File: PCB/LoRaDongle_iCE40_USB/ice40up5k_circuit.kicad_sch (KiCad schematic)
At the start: 41 parts, among them IC3 SGP40-D-R4, J3 Conn_01x08_Male, J4 Conn_01x04_Male, J6 Conn_02x02_Top_Bottom, J9 Conn_01x17_Male, SW1 SW_Push, SW2 SW_Push, U5 W25Q128JVS, U6 ICE40UP5K-SG48ITR, X1 ECS-2520MV-500-BL-TR

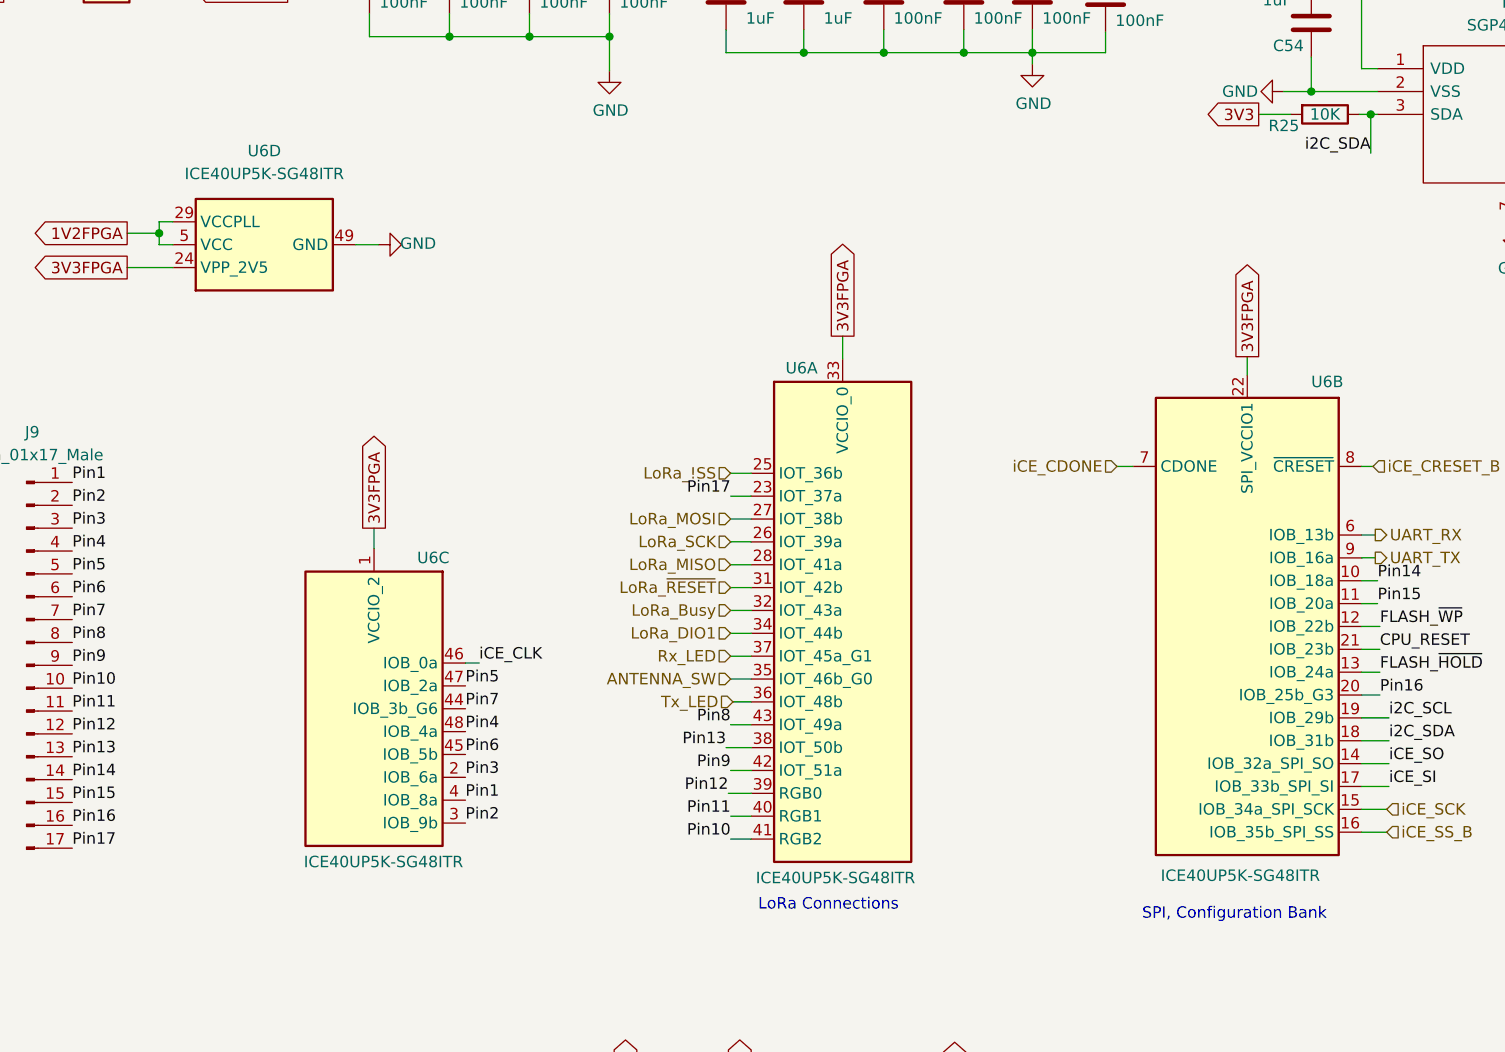
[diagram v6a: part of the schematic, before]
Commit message: updated silkscreen
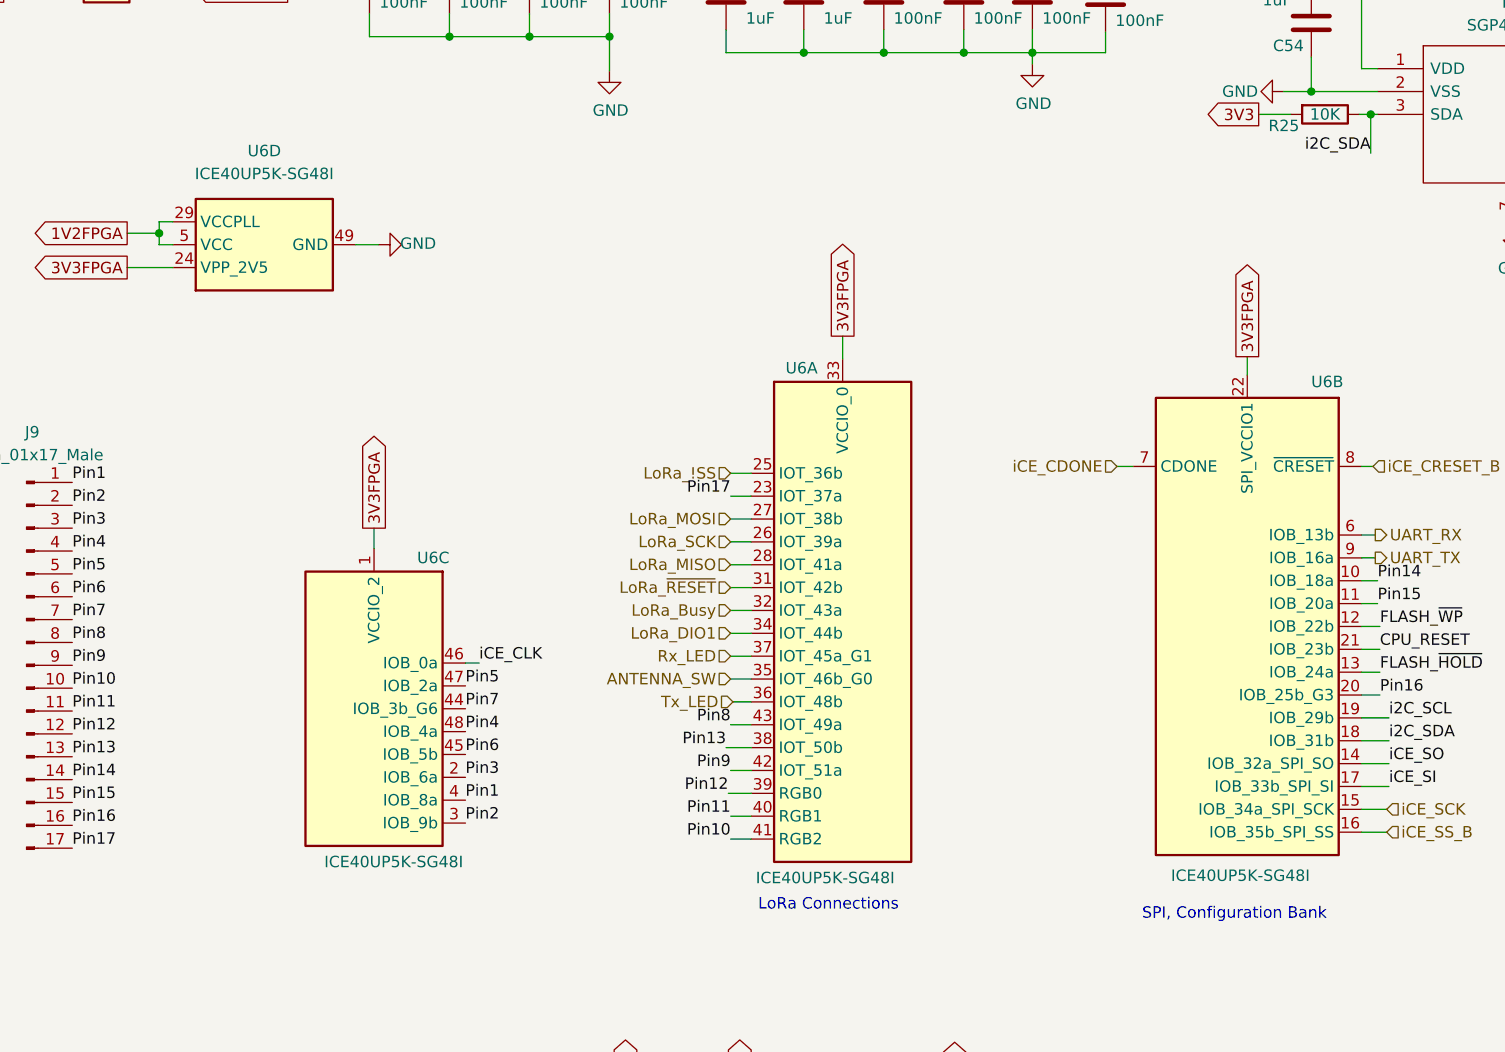
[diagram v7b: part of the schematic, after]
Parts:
- D2, IC3, R12, R13, R14, R15, R16, R17, R24, R25, R26, R27, U5: Type (none) -> SMD
- J3, J4, J9: Type (none) -> Through Hole
- J6: Type (none) -> Through hole
- U6: value ICE40UP5K-SG48ITR -> ICE40UP5K-SG48I; Manufacturer Part Number ICE40UP5K-SG48ITR50 -> ICE40UP5K-SG48IT; Type (none) -> SMD
- iCE_CLK1: Type (none) -> -
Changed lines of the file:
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@@
+      (effects (font (size 1.27 1.27)) hide)
+    )
+    (property "Type" "SMD" (id 8) (at 107.696 164.592 0)
       (effects (font (size 1.27 1.27)) hide)
     )
@@
       (effects (font (size 1.27 1.27)) hide)
     )
+    (property "Type" "SMD" (id 8) (at 94.996 164.592 0)
+      (effects (font (size 1.27 1.27)) hide)
+    )
     (pin "1")
     (pin "2")
@@
     )
     (property "Package" "0603" (id 7) (at 94.996 181.102 0)
+      (effects (font (size 1.27 1.27)) hide)
+    )
+    (property "Type" "SMD" (id 8) (at 94.996 181.102 0)
       (effects (font (size 1.27 1.27)) hide)
     )
@@
       (effects (font (size 1.27 1.27)) hide)
     )
+    (property "Type" "SMD" (id 8) (at 220.98 85.852 0)
+      (effects (font (size 1.27 1.27)) hide)
+    )
     (pin "1")
     (pin "2")
@@
       (effects (font (size 1.27 1.27)) hide)
     )
+    (property "Type" "SMD" (id 8) (at 271.272 102.362 0)
+      (effects (font (size 1.27 1.27)) hide)
+    )
     (pin "1")
     (pin "2")
@@
       (effects (font (size 1.27 1.27)) hide)
     )
+    (property "Type" "SMD" (id 8) (at 271.272 99.822 0)
+      (effects (font (size 1.27 1.27)) hide)
+    )
     (pin "1")
     (pin "2")
@@
       (effects (font (size 1.27 1.27)) hide)
     )
+    (property "Type" "SMD" (id 8) (at 225.552 85.852 0)
+      (effects (font (size 1.27 1.27)) hide)
+    )
     (pin "1")
     (pin "2")
@@
       (effects (font (size 1.27 1.27)) (justify left))
     )
-    (property "Value" "ICE40UP5K-SG48ITR" (id 1) (at 109.474 133.35 0)
+    (property "Value" "ICE40UP5K-SG48I" (id 1) (at 109.474 133.35 0)
       (effects (font (size 1.27 1.27)) (justify left))
     )
@@
       (effects (font (size 1.27 1.27)) hide)
     )
-    (property "Manufacturer Part Number" "ICE40UP5K-SG48ITR50" (id 5) (at 119.126 103.632 0)
+    (property "Manufacturer Part Number" "ICE40UP5K-SG48IT" (id 5) (at 119.126 103.632 0)
       (effects (font (size 1.27 1.27)) hide)
     )
     (property "Package" "48-QFN" (id 6) (at 119.126 103.632 0)
+      (effects (font (size 1.27 1.27)) hide)
+    )
+    (property "Type" "SMD" (id 7) (at 119.126 103.632 0)
       (effects (font (size 1.27 1.27)) hide)
     )
@@
       (effects (font (size 1.27 1.27)) hide)
     )
+    (property "Type" "SMD" (id 8) (at 214.376 36.576 0)
+      (effects (font (size 1.27 1.27)) hide)
+    )
     (pin "1")
     (pin "2")
@@
       (effects (font (size 1.27 1.27)) hide)
     )
+    (property "Type" "Through hole" (id 8) (at 36.068 32.258 0)
+      (effects (font (size 1.27 1.27)) hide)
+    )
     (pin "1")
     (pin "2")
@@
     (in_bom yes) (on_board yes)
     (property "Reference" "U6" (id 0) (at 172.974 78.232 0))
-    (property "Value" "ICE40UP5K-SG48ITR" (id 1) (at 163.322 133.096 0))
+    (property "Value" "ICE40UP5K-SG48I" (id 1) (at 163.322 133.096 0))
     (property "Footprint" "Package_DFN_QFN:QFN-48-1EP_7x7mm_P0.5mm_EP5.6x5.6mm" (id 2) (at 164.084 139.7 0)
       (effects (font (size 1.27 1.27)) hide)
@@
       (effects (font (size 1.27 1.27)) hide)
     )
-    (property "Manufacturer Part Number" "ICE40UP5K-SG48ITR50" (id 5) (at 164.084 105.41 0)
+    (property "Manufacturer Part Number" "ICE40UP5K-SG48IT" (id 5) (at 164.084 105.41 0)
       (effects (font (size 1.27 1.27)) hide)
     )
     (property "Package" "48-QFN" (id 6) (at 164.084 105.41 0)
+      (effects (font (size 1.27 1.27)) hide)
+    )
+    (property "Type" "SMD" (id 7) (at 164.084 105.41 0)
       (effects (font (size 1.27 1.27)) hide)
     )
@@
     (in_bom yes) (on_board yes) (fields_autoplaced)
     (property "Reference" "U6" (id 0) (at 54.864 52.578 90))
-    (property "Value" "ICE40UP5K-SG48ITR" (id 1) (at 54.864 55.118 90))
+    (property "Value" "ICE40UP5K-SG48I" (id 1) (at 54.864 55.118 90))
     (property "Footprint" "Package_DFN_QFN:QFN-48-1EP_7x7mm_P0.5mm_EP5.6x5.6mm" (id 2) (at 89.154 62.992 0)
       (effects (font (size 1.27 1.27)) hide)
@@
       (effects (font (size 1.27 1.27)) hide)
     )
-    (property "Manufacturer Part Number" "ICE40UP5K-SG48ITR50" (id 5) (at 54.864 62.992 0)
+    (property "Manufacturer Part Number" "ICE40UP5K-SG48IT" (id 5) (at 54.864 62.992 0)
       (effects (font (size 1.27 1.27)) hide)
     )
     (property "Package" "48-QFN" (id 6) (at 54.864 62.992 0)
+      (effects (font (size 1.27 1.27)) hide)
+    )
+    (property "Type" "SMD" (id 7) (at 54.864 62.992 0)
       (effects (font (size 1.27 1.27)) hide)
     )
@@
       (effects (font (size 1.27 1.27)) hide)
     )
+    (property "Type" "SMD" (id 8) (at 176.784 29.21 0)
+      (effects (font (size 1.27 1.27)) hide)
+    )
     (pin "1")
     (pin "2")
@@
       (effects (font (size 1.27 1.27)) hide)
     )
+    (property "Type" "Through Hole" (id 8) (at 267.462 29.464 0)
+      (effects (font (size 1.27 1.27)) hide)
+    )
     (pin "1")
     (pin "2")
@@
       (effects (font (size 1.27 1.27)) (justify left))
     )
-    (property "Value" "ICE40UP5K-SG48ITR" (id 1) (at 76.962 131.572 0)
+    (property "Value" "ICE40UP5K-SG48I" (id 1) (at 76.962 131.572 0)
       (effects (font (size 1.27 1.27)) (justify left))
     )
@@
       (effects (font (size 1.27 1.27)) hide)
     )
-    (property "Manufacturer Part Number" "ICE40UP5K-SG48ITR50" (id 5) (at 67.056 114.554 0)
+    (property "Manufacturer Part Number" "ICE40UP5K-SG48IT" (id 5) (at 67.056 114.554 0)
       (effects (font (size 1.27 1.27)) hide)
     )
     (property "Package" "48-QFN" (id 6) (at 67.056 114.554 0)
+      (effects (font (size 1.27 1.27)) hide)
+    )
+    (property "Type" "SMD" (id 7) (at 67.056 114.554 0)
       (effects (font (size 1.27 1.27)) hide)
     )
@@
       (effects (font (size 1.27 1.27)) hide)
     )
+    (property "Type" "SMD" (id 8) (at 242.062 97.282 0)
+      (effects (font (size 1.27 1.27)) hide)
+    )
     (pin "1")
     (pin "2")
@@
       (effects (font (size 1.27 1.27)) hide)
     )
+    (property "Type" "SMD" (id 8) (at 131.572 164.846 0)
+      (effects (font (size 1.27 1.27)) hide)
+    )
     (pin "1")
     (pin "2")
@@
     )
     (property "Package" "-" (id 7) (at 28.448 109.728 0)
+      (effects (font (size 1.27 1.27)) hide)
+    )
+    (property "Type" "Through Hole" (id 8) (at 28.448 109.728 0)
       (effects (font (size 1.27 1.27)) hide)
     )
@@
       (effects (font (size 1.27 1.27)) hide)
     )
+    (property "Type" "Through Hole" (id 8) (at 240.792 34.036 0)
+      (effects (font (size 1.27 1.27)) hide)
+    )
     (pin "1")
     (pin "2")
@@
       (effects (font (size 1.27 1.27)) hide)
     )
+    (property "Type" "SMD" (id 8) (at 172.72 48.514 0)
+      (effects (font (size 1.27 1.27)) hide)
+    )
     (pin "1")
     (pin "2")
@@
       (effects (font (size 1.27 1.27)) hide)
     )
+    (property "Type" "SMD" (id 15) (at 178.562 43.434 0)
+      (effects (font (size 1.27 1.27)) hide)
+    )
     (pin "1")
     (pin "2")
@@
       (effects (font (size 1.27 1.27)) hide)
     )
+    (property "Type" "-" (id 8) (at 59.182 176.784 0)
+      (effects (font (size 1.27 1.27)) hide)
+    )
